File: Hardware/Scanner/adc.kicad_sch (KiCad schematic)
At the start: 8 parts, among them U2 NAU7802SGI, X1 4.9152 MHz

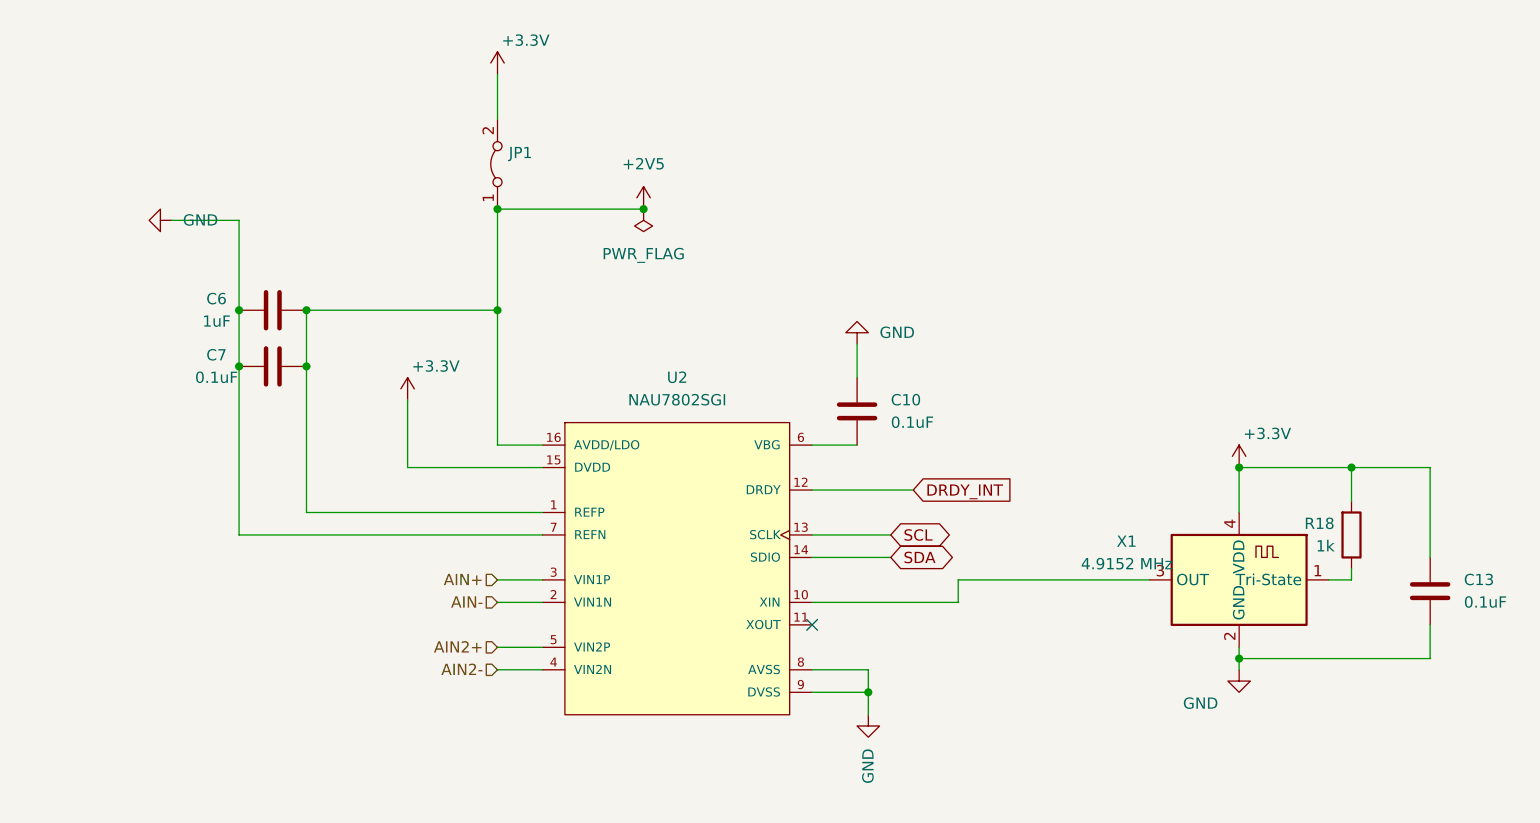
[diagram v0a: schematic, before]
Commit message: added footprint for MTSM2601SMF1-100
Signed-off-by: lokimetasmith <lokimail@gmail.com>
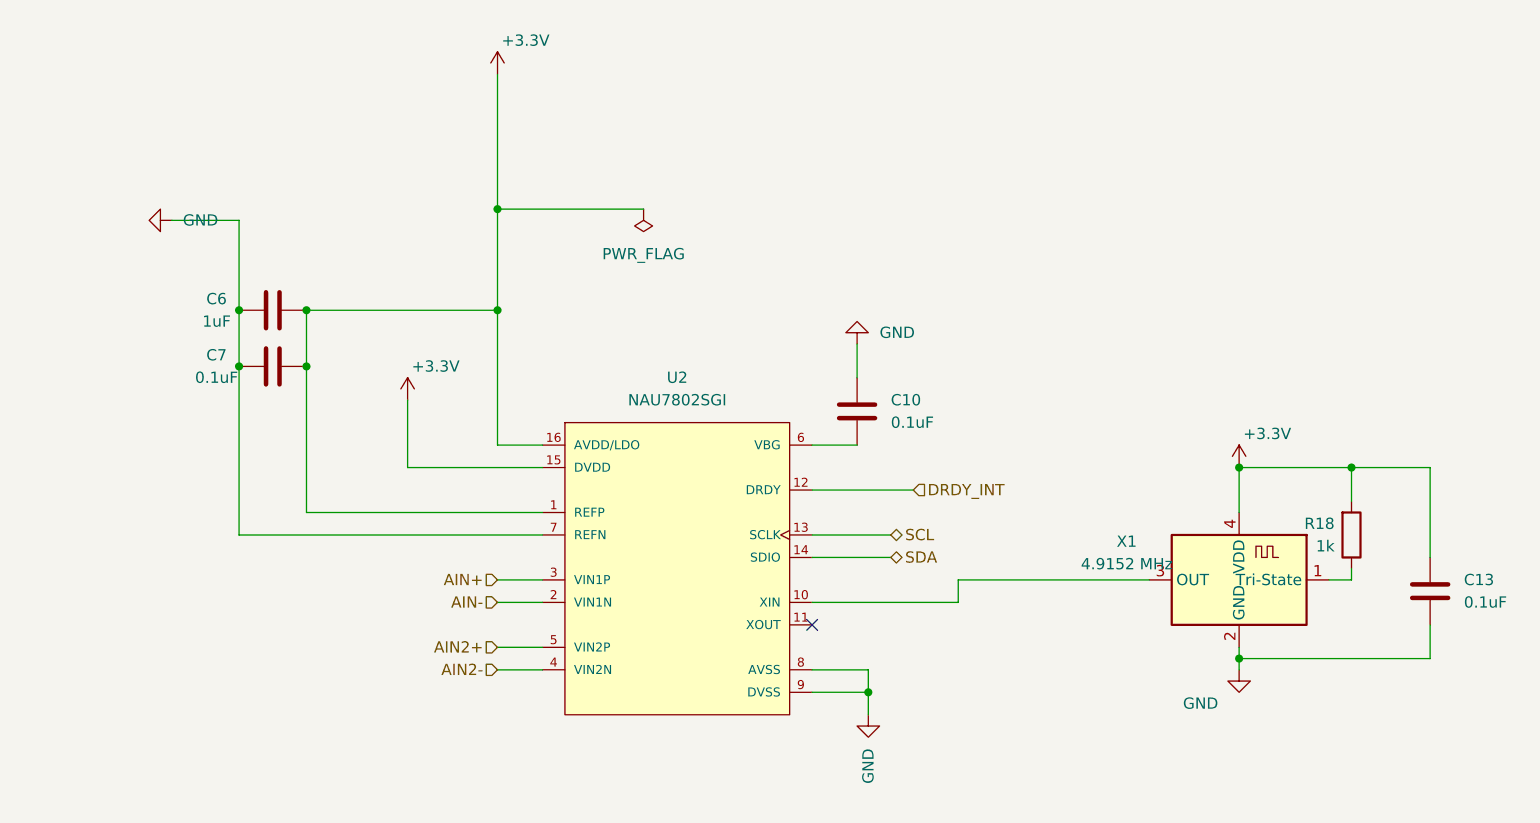
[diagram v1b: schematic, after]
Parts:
- removed JP1: (no value), symbol Jumper:Jumper_2_Bridged
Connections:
- net +2V5 is gone; now on net +3V3: C6.2, C7.2, U2.1 (REFP), U2.16 (AVDD/LDO)

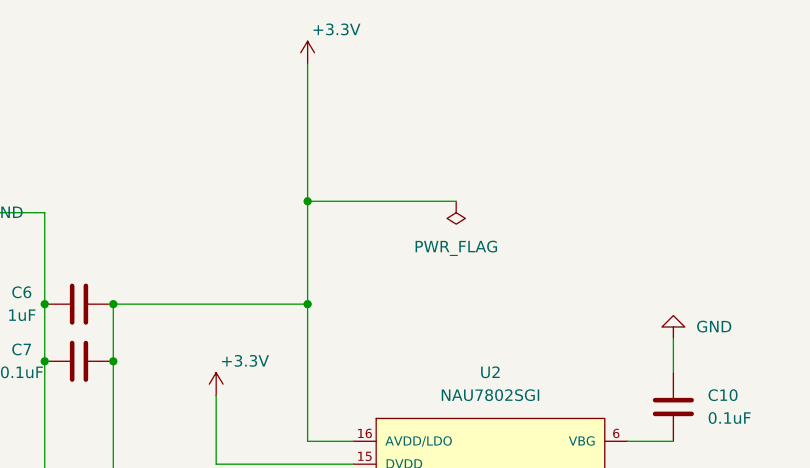
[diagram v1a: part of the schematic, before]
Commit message: lots of changes, added footprints, fixed broken schemaitcs, fixed kicad 7.0 issues
Signed-off-by: lokimetasmith <lokimail@gmail.com>
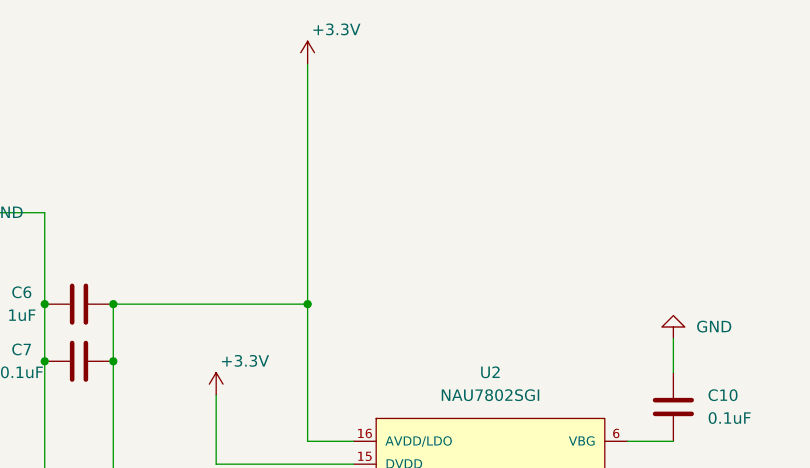
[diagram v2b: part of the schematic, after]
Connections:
- net +3V3 renamed +3.3V
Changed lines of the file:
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@@
   (junction (at 107.95 88.9) (diameter 0) (color 0 0 0 0)
-  )
-  (junction (at 137.16 71.12) (diameter 0) (color 0 0 0 0)
   )
   (junction (at 107.95 82.55) (diameter 0) (color 0 0 0 0)
@@
     (stroke (width 0) (type default))
   )
-  (wire (pts (xy 137.16 71.12) (xy 153.67 71.12))
-    (stroke (width 0) (type default))
-  )
   (wire (pts (xy 107.95 107.95) (xy 107.95 88.9))
     (stroke (width 0) (type default))
@@
     (stroke (width 0) (type default))
   )
-  (wire (pts (xy 137.16 55.88) (xy 137.16 71.12))
+  (wire (pts (xy 137.16 55.88) (xy 137.16 82.55))
     (stroke (width 0) (type default))
   )
@@
   )
   (wire (pts (xy 107.95 82.55) (xy 107.95 88.9))
-    (stroke (width 0) (type default))
-  )
-  (wire (pts (xy 137.16 71.12) (xy 137.16 82.55))
     (stroke (width 0) (type default))
   )
@@
         )
       )
-    )
-  )
-  (symbol (lib_id "power:PWR_FLAG") (at 153.67 71.12 0) (mirror x) (unit 1)
-    (in_bom yes) (on_board yes) (dnp no) (fields_autoplaced)
-    (property "Reference" "#FLG0101" (at 153.67 73.025 0)
-      (effects (font (size 1.27 1.27)) hide)
-    )
-    (property "Value" "PWR_FLAG" (at 153.67 76.2 0)
-      (effects (font (size 1.27 1.27)))
-    )
-    (property "Footprint" "" (at 153.67 71.12 0)
-      (effects (font (size 1.27 1.27)) hide)
-    )
-    (property "Datasheet" "~" (at 153.67 71.12 0)
-      (effects (font (size 1.27 1.27)) hide)
-    )
-    (pin "1")
-    (instances
-      (project "RoundScanner"
-        (path "/a818e058-3544-4da8-96fb-1a428660711f/a8dcb7a4-48cf-403e-b881-d44234291c62"
-          (reference "#FLG0101") (unit 1)
-        )
-      )

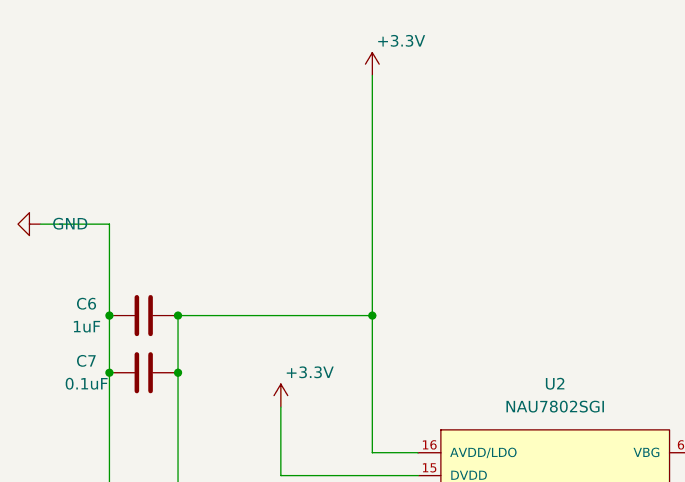
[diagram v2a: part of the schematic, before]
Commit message: added options for using internal adc, external adc, or 3.3v
Signed-off-by: lokimetasmith <lokimail@gmail.com>
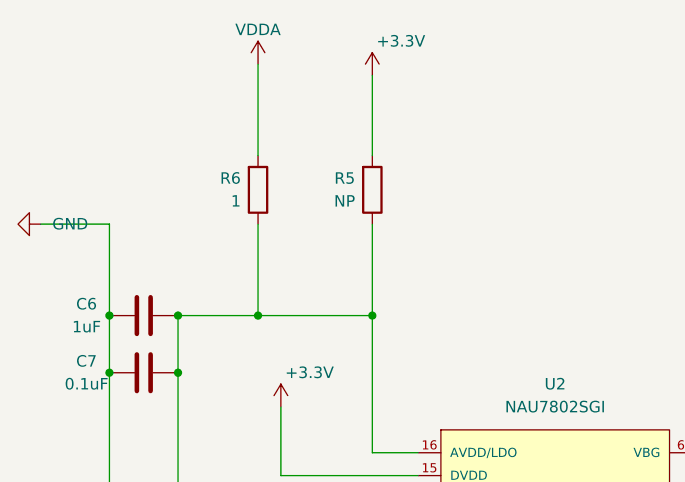
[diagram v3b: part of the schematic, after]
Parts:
- added R5: NP, Resistor_SMD:R_0603_1608Metric_Pad0.98x0.95mm_HandSolder, symbol Device:R
- added R6: 1, Resistor_SMD:R_0603_1608Metric_Pad0.98x0.95mm_HandSolder, symbol Device:R
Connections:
- net +3.3V: now also R5.2; no longer C6.2, C7.2, U2.1 (REFP), U2.16 (AVDD/LDO)
- new net: C6.2, C7.2, R5.1, R6.1, U2.1 (REFP), U2.16 (AVDD/LDO)
- new net VDDA: R6.2
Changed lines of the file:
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@@
   (junction (at 115.57 88.9) (diameter 0) (color 0 0 0 0)
   )
+  (junction (at 115.57 82.55) (diameter 0) (color 0 0 0 0)
+  )
   (junction (at 137.16 82.55) (diameter 0) (color 0 0 0 0)
   )
-  (junction (at 115.57 82.55) (diameter 0) (color 0 0 0 0)
-  )
   (junction (at 220.98 100.33) (diameter 0) (color 0 0 0 0)
   )
@@
   )
   (junction (at 107.95 88.9) (diameter 0) (color 0 0 0 0)
+  )
+  (junction (at 124.46 82.55) (diameter 0) (color 0 0 0 0)
   )
   (junction (at 107.95 82.55) (diameter 0) (color 0 0 0 0)
@@
     (stroke (width 0) (type default))
   )
-  (wire (pts (xy 115.57 82.55) (xy 137.16 82.55))
+  (wire (pts (xy 115.57 82.55) (xy 124.46 82.55))
     (stroke (width 0) (type default))
   )
@@
     (stroke (width 0) (type default))
   )
+  (wire (pts (xy 124.46 54.61) (xy 124.46 64.77))
+    (stroke (width 0) (type default))
+  )
   (wire (pts (xy 177.8 86.36) (xy 177.8 90.17))
     (stroke (width 0) (type default))
@@
     (stroke (width 0) (type default))
   )
-  (wire (pts (xy 137.16 55.88) (xy 137.16 82.55))
+  (wire (pts (xy 124.46 82.55) (xy 137.16 82.55))
     (stroke (width 0) (type default))
   )
@@
     (stroke (width 0) (type default))
   )
+  (wire (pts (xy 124.46 72.39) (xy 124.46 82.55))
+    (stroke (width 0) (type default))
+  )
   (wire (pts (xy 220.98 121.92) (xy 220.98 123.19))
     (stroke (width 0) (type default))
@@
     (stroke (width 0) (type default))
   )
+  (wire (pts (xy 137.16 72.39) (xy 137.16 82.55))
+    (stroke (width 0) (type default))
+  )
   (wire (pts (xy 127 92.71) (xy 127 100.33))
     (stroke (width 0) (type default))
@@
   )
   (wire (pts (xy 137.16 113.03) (xy 142.24 113.03))
+    (stroke (width 0) (type default))
+  )
+  (wire (pts (xy 137.16 55.88) (xy 137.16 64.77))
     (stroke (width 0) (type default))
   )
@@
     )
   )
+  (symbol (lib_id "Device:R") (at 137.16 68.58 0) (mirror x) (unit 1)
+    (in_bom yes) (on_board yes) (dnp no)
+    (property "Reference" "R5" (at 135.255 67.3099 0)
+      (effects (font (size 1.27 1.27)) (justify right))
+    )
+    (property "Value" "NP" (at 135.255 69.8499 0)
+      (effects (font (size 1.27 1.27)) (justify right))
+    )
+    (property "Footprint" "Resistor_SMD:R_0603_1608Metric_Pad0.98x0.95mm_HandSolder" (at 135.382 68.58 90)
+      (effects (font (size 1.27 1.27)) hide)
+    )
+    (property "Datasheet" "~" (at 137.16 68.58 0)
+      (effects (font (size 1.27 1.27)) hide)
+    )
+    (pin "1")
+    (pin "2")
+    (instances
+      (project "RoundScanner"
+        (path "/a818e058-3544-4da8-96fb-1a428660711f/a8dcb7a4-48cf-403e-b881-d44234291c62"
+          (reference "R5") (unit 1)
+        )
+      )
+    )
+  )
   (symbol (lib_id "power:+3.3V") (at 137.16 55.88 0) (unit 1)
     (in_bom yes) (on_board yes) (dnp no)
@@
         (path "/a818e058-3544-4da8-96fb-1a428660711f/a8dcb7a4-48cf-403e-b881-d44234291c62"
           (reference "#PWR0133") (unit 1)
+        )
+      )
+    )
+  )
+  (symbol (lib_id "Device:R") (at 124.46 68.58 0) (mirror x) (unit 1)
+    (in_bom yes) (on_board yes) (dnp no)
+    (property "Reference" "R6" (at 122.555 67.3099 0)
+      (effects (font (size 1.27 1.27)) (justify right))
+    )
+    (property "Value" "1" (at 122.555 69.8499 0)
+      (effects (font (size 1.27 1.27)) (justify right))
+    )
+    (property "Footprint" "Resistor_SMD:R_0603_1608Metric_Pad0.98x0.95mm_HandSolder" (at 122.682 68.58 90)
+      (effects (font (size 1.27 1.27)) hide)
+    )
+    (property "Datasheet" "~" (at 124.46 68.58 0)
+      (effects (font (size 1.27 1.27)) hide)
+    )
+    (pin "1")
+    (pin "2")
+    (instances
+      (project "RoundScanner"
+        (path "/a818e058-3544-4da8-96fb-1a428660711f/a8dcb7a4-48cf-403e-b881-d44234291c62"
+          (reference "R6") (unit 1)
         )
       )
@@
         )
       )
+    )
+  )
+  (symbol (lib_id "power:VDDA") (at 124.46 54.61 0) (unit 1)
+    (in_bom yes) (on_board yes) (dnp no) (fields_autoplaced)
+    (property "Reference" "#PWR014" (at 124.46 58.42 0)
+      (effects (font (size 1.27 1.27)) hide)
+    )
+    (property "Value" "VDDA" (at 124.46 50.8 0)
+      (effects (font (size 1.27 1.27)))
+    )
+    (property "Footprint" "" (at 124.46 54.61 0)
+      (effects (font (size 1.27 1.27)) hide)
+    )
+    (property "Datasheet" "" (at 124.46 54.61 0)
+      (effects (font (size 1.27 1.27)) hide)
+    )
+    (pin "1")
+    (instances
+      (project "RoundScanner"
+        (path "/a818e058-3544-4da8-96fb-1a428660711f/5869e7b3-0d61-455b-97ad-e4e8b4829f27"
+          (reference "#PWR014") (unit 1)
+        )
+        (path "/a818e058-3544-4da8-96fb-1a428660711f/a8dcb7a4-48cf-403e-b881-d44234291c62"
+          (reference "#PWR018") (unit 1)
+        )
+      )
